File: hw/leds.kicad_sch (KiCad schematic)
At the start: 28 parts, among them Q4 SSM6N35AFE

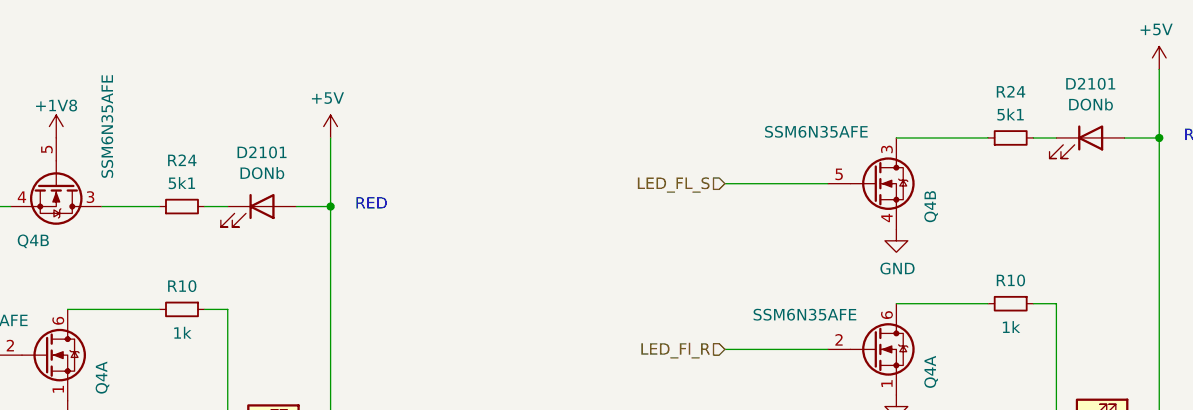
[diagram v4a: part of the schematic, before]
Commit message: Added trion top-sheet as sub-sheet to usbadc project
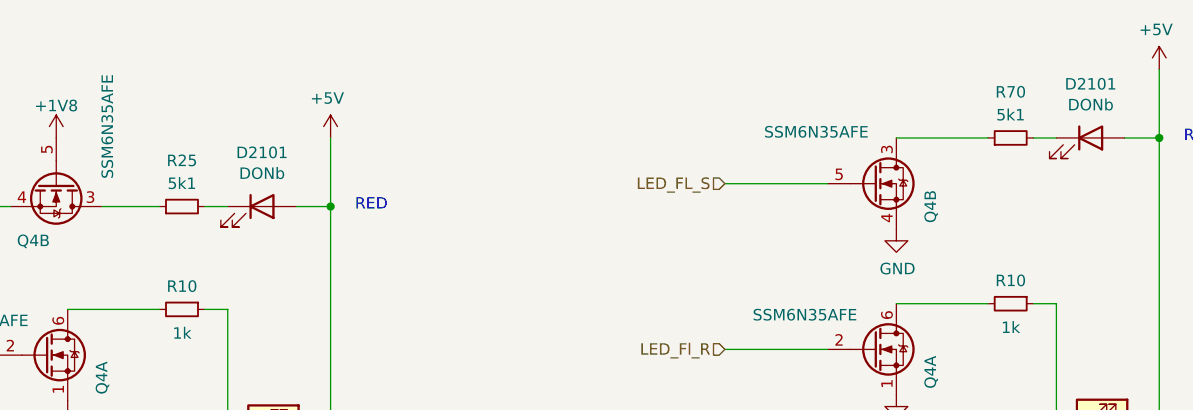
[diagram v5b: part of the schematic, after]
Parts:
- renumbered R24 to R25, R24 to R70

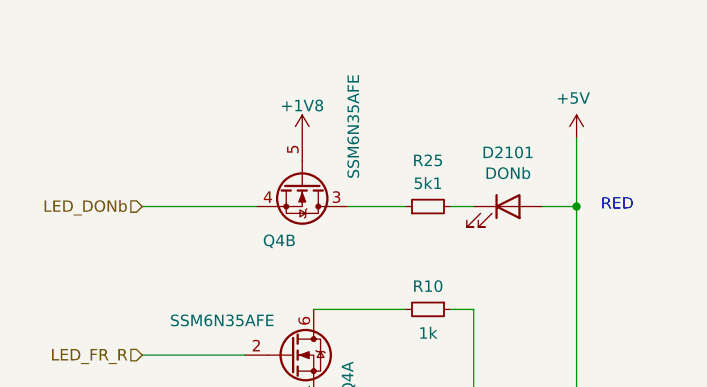
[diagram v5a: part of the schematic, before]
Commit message: moved trion into place; going to 'hide' footprint reference designators...
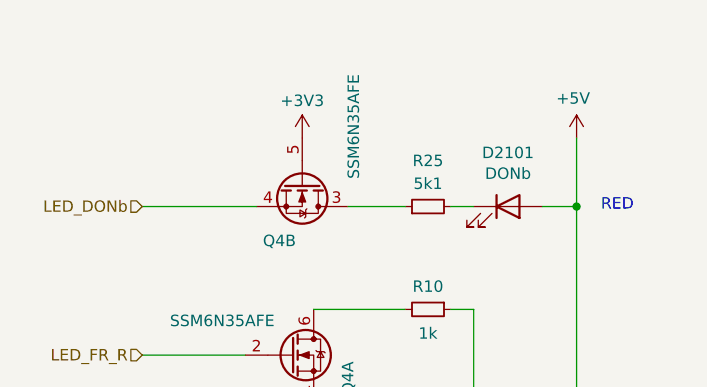
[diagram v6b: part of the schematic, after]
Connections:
- net +1V8 renamed +3V3
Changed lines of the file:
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@@
-    )
-  )
-  (symbol (lib_id "power:+1V8") (at 81.915 32.385 0) (unit 1)
-    (in_bom yes) (on_board yes) (dnp no)
-    (property "Reference" "#PWR0177" (at 81.915 36.195 0)
-      (effects (font (size 1.27 1.27)) hide)
-    )
-    (property "Value" "+1V8" (at 81.915 28.829 0)
-      (effects (font (size 1.27 1.27)))
-    )
-    (property "Footprint" "" (at 81.915 32.385 0)
-      (effects (font (size 1.27 1.27)) hide)
-    )
-    (property "Datasheet" "" (at 81.915 32.385 0)
-      (effects (font (size 1.27 1.27)) hide)
-    )
-    (pin "1")
-    (instances
-      (project "usbadc"
-        (path "/7c8a1f8d-8834-4c9b-aaae-1f231e9b09a1/33541e06-1943-44ac-875f-55941863f921"
-          (reference "#PWR0177") (unit 1)
-        )
-      )
     )
   )
@@
         )
       )
+    )
+  )
+  (symbol (lib_id "power:+3V3") (at 81.915 32.385 0) (unit 1)
+    (in_bom yes) (on_board yes) (dnp no) (fields_autoplaced)
+    (property "Reference" "#PWR0102" (at 81.915 36.195 0)
+      (effects (font (size 1.27 1.27)) hide)
+    )
+    (property "Value" "+3V3" (at 81.915 28.2519 0)
+      (effects (font (size 1.27 1.27)))
+    )
+    (property "Footprint" "" (at 81.915 32.385 0)
+      (effects (font (size 1.27 1.27)) hide)
+    )
+    (property "Datasheet" "" (at 81.915 32.385 0)
+      (effects (font (size 1.27 1.27)) hide)
+    )
+    (pin "1")
+    (instances
+      (project "usbadc"
+        (path "/7c8a1f8d-8834-4c9b-aaae-1f231e9b09a1/33541e06-1943-44ac-875f-55941863f921"
+          (reference "#PWR0102") (unit 1)
+        )
+      )

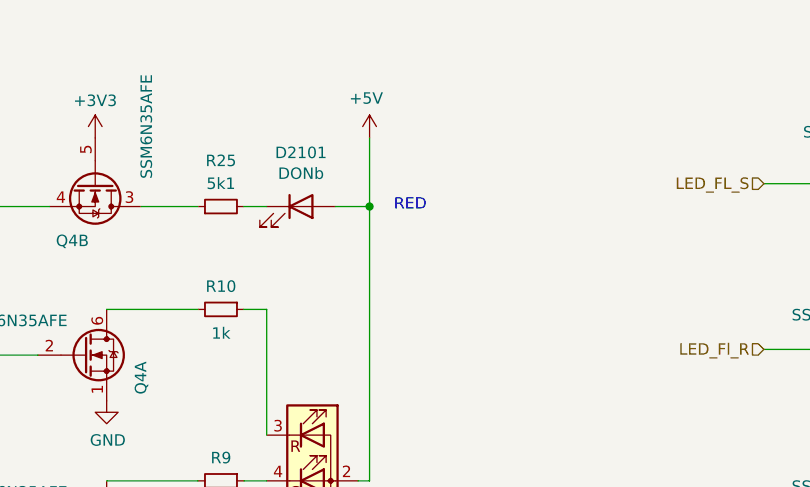
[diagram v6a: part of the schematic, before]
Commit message: layout almost complete with UPLI on the RHS => NO CLOCK INPUT
Have to rework and move the usb transceiver to the left...
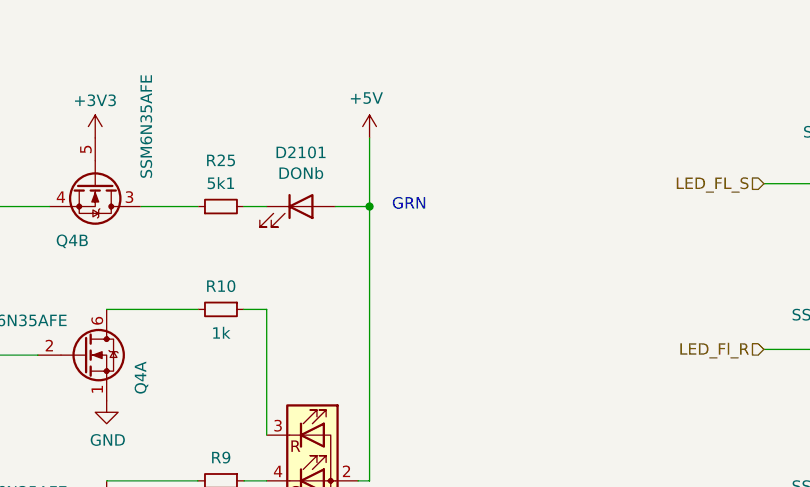
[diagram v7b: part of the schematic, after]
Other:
- note added: "GRN"
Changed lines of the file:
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@@
     (stroke (width 0) (type default))
   )
-  (text "RED" (at 118.745 40.64 0)
+  (text "GRN" (at 118.745 40.64 0)
     (effects (font (size 1.27 1.27)) (justify right bottom))
   )

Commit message: finalizing...
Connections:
- net LED_Fl_R is gone; now on net LED_FR_R: Q4.2 (G)
- net LED_FL_B: now also Q4.5 (G); no longer Q4.5 (G)
- net LED_FL_G: now also Q4.2 (G); no longer Q4.2 (G)
- net LED_FR_B: now also Q4.5 (G); no longer Q4.5 (G)
- net LED_FR_G: now also Q4.2 (G); no longer Q4.2 (G)
- net LED_FR_R: no longer Q4.2 (G)
- net LED_FL_S renamed LED_FR_S
- new net LED_FL_R: Q4.2 (G)
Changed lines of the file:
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@@
     (effects (font (size 1.27 1.27)) (justify right))
   )
-  (hierarchical_label "LED_FR_B" (shape input) (at 64.135 94.615 180) (fields_autoplaced)
+  (hierarchical_label "LED_FR_B" (shape input) (at 156.21 93.98 180) (fields_autoplaced)
     (effects (font (size 1.27 1.27)) (justify right))
   )
@@
     (effects (font (size 1.27 1.27)) (justify right))
   )
-  (hierarchical_label "LED_FL_B" (shape input) (at 156.21 93.98 180) (fields_autoplaced)
+  (hierarchical_label "LED_FL_B" (shape input) (at 64.135 94.615 180) (fields_autoplaced)
     (effects (font (size 1.27 1.27)) (justify right))
   )
-  (hierarchical_label "LED_FL_S" (shape input) (at 156.21 37.465 180) (fields_autoplaced)
+  (hierarchical_label "LED_FR_S" (shape input) (at 156.21 37.465 180) (fields_autoplaced)
     (effects (font (size 1.27 1.27)) (justify right))
   )
@@
     (effects (font (size 1.27 1.27)) (justify right))
   )
-  (hierarchical_label "LED_FL_G" (shape input) (at 156.21 74.93 180) (fields_autoplaced)
+  (hierarchical_label "LED_FL_G" (shape input) (at 64.135 75.565 180) (fields_autoplaced)
     (effects (font (size 1.27 1.27)) (justify right))
   )
-  (hierarchical_label "LED_Fl_R" (shape input) (at 156.21 55.88 180) (fields_autoplaced)
+  (hierarchical_label "LED_FL_R" (shape input) (at 64.135 56.515 180) (fields_autoplaced)
     (effects (font (size 1.27 1.27)) (justify right))
   )
-  (hierarchical_label "LED_FR_R" (shape input) (at 64.135 56.515 180) (fields_autoplaced)
+  (hierarchical_label "LED_FR_R" (shape input) (at 156.21 55.88 180) (fields_autoplaced)
     (effects (font (size 1.27 1.27)) (justify right))
   )
@@
     (effects (font (size 1.27 1.27)) (justify right))
   )
-  (hierarchical_label "LED_FR_G" (shape input) (at 64.135 75.565 180) (fields_autoplaced)
+  (hierarchical_label "LED_FR_G" (shape input) (at 156.21 74.93 180) (fields_autoplaced)
     (effects (font (size 1.27 1.27)) (justify right))
   )
